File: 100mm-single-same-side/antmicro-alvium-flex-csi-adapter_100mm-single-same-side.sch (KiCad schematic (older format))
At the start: 2 parts, among them J1 WE_687622100002_FLEX, J2 WE_687650100002_FLEX

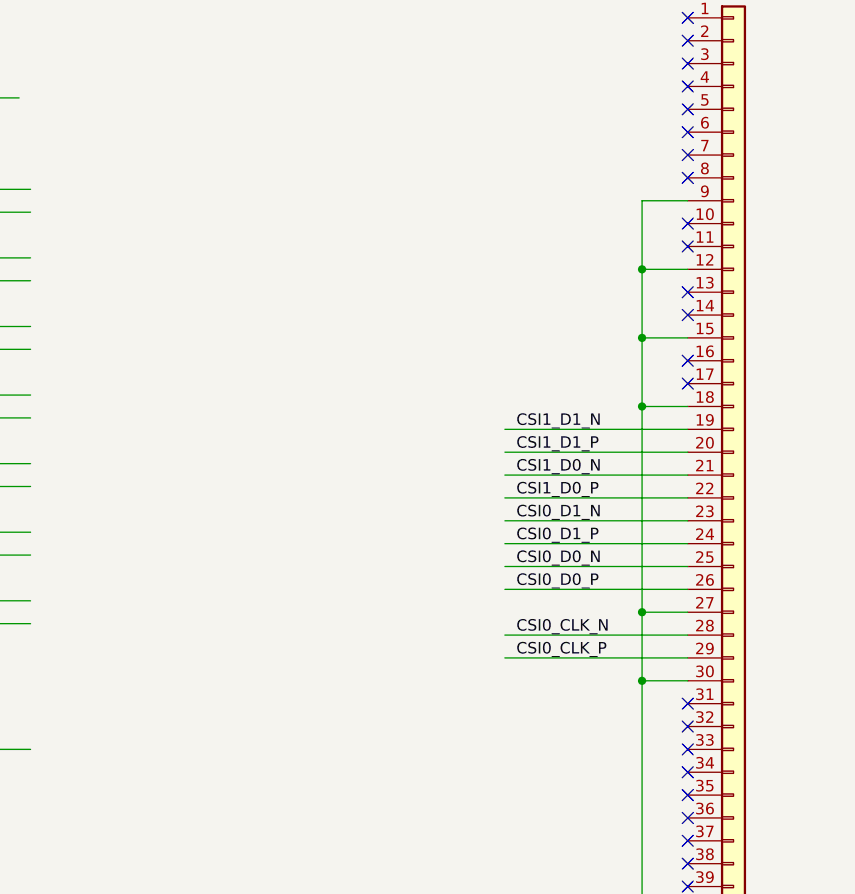
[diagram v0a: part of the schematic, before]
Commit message: Add NMOS transistor for camera triggering in 100mm single same side variant
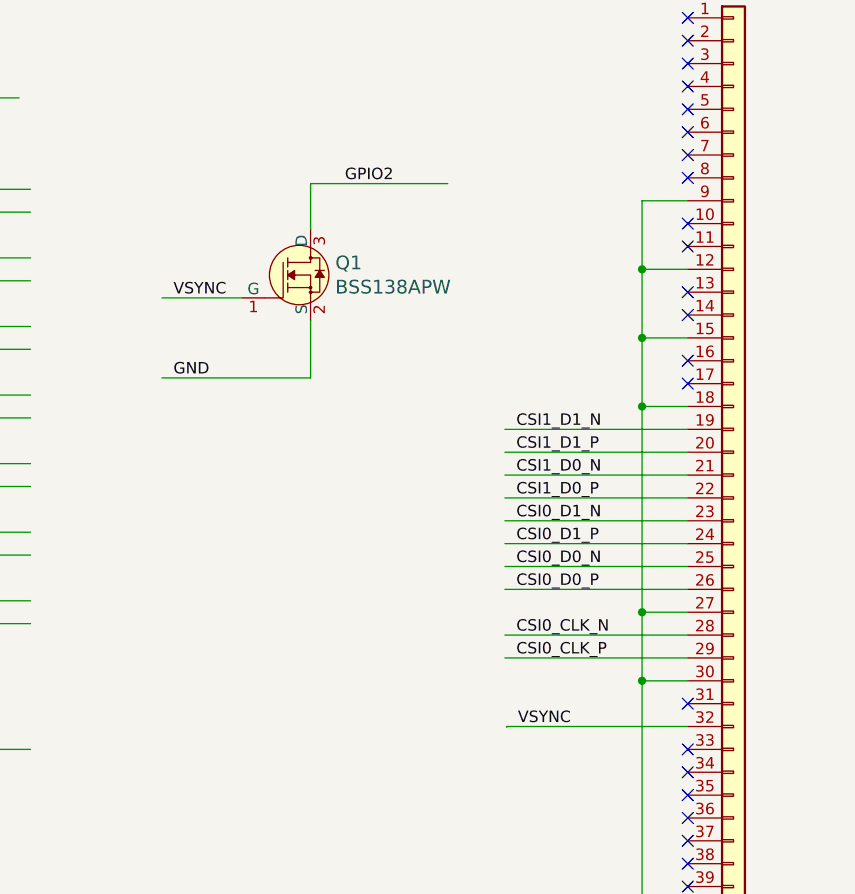
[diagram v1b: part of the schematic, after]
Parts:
- added Q1: BSS138APW, antmicro-alvium-flex-csi-adapter-footprints:SC70-3, symbol antmicro-alvium-flex-csi-adapter:BSS138APW
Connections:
- net labels added: VSYNC
- wire segments 61 -> 68
- no-connect marks 30 -> 29
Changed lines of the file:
@@
 Text Notes 825  2100 0    79   ~ 16
 FFC contacts - Alvium side
-NoConn ~ 5250 5425
 Text Notes 4925 2050 0    79   ~ 16
 FFC contacts - Antmicro side
@@
 Text Label 1925 3075 0    50   ~ 0
 SCL
+$Comp
+L antmicro-alvium-flex-csi-adapter:BSS138APW Q1
+U 1 1 5F92A017
+P 3600 3450
+F 0 "Q1" H 3708 3503 60  0000 L CNN
+F 1 "BSS138APW" H 3708 3397 60  0000 L CNN
+F 2 "antmicro-alvium-flex-csi-adapter-footprints:SC70-3" H 3800 3650 60  0001 L CNN
+F 3 "" H 3800 3750 60  0001 L CNN
+F 4 "BSS138PW" H 3800 3950 60  0001 L CNN "MPN"
+F 5 "ON Semiconductor" H 3800 4550 60  0001 L CNN "Manufacturer"
+	1    3600 3450
+	1    0    0    -1
+$EndComp
+Wire Wire Line
+	3600 3650 3600 3900
+Wire Wire Line
+	3600 3900 2950 3900
+Wire Wire Line
+	3300 3550 2950 3550
+Wire Wire Line
+	3600 3250 3600 3050
+Wire Wire Line
+	3600 3050 4200 3050
+Text Label 3750 3050 0    50   ~ 0
+GPIO2
+Text Label 3000 3900 0    50   ~ 0
+GND
+Text Label 4507 5425 0    50   ~ 0
+VSYNC
+Text Label 3000 3550 0    50   ~ 0
+VSYNC
+Wire Wire Line
+	5250 5425 4458 5425
+Wire Wire Line
+	4458 5425 4458 5428
 $EndSCHEMATC

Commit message: 100mm-single-same: update signage
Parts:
- added N1: oshw_logo, antmicro-alvium-flex-csi-adapter-footprints:oshw-logo, symbol antmicro-alvium-flex-csi-adapter:oshw_logo
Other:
- note added: "Alvium Camera"
- note added: "Alvium flex CSI adapter 100mm single same side contacts"
- note added: "Antmicro CSI interface"
- note removed: "Antmicro - Alvium Flex CSI Adapter"
- note removed: "FFC contacts - Alvium side"
- note removed: "FFC contacts - Antmicro side"
- moved on the sheet: J1, J2, Q1
